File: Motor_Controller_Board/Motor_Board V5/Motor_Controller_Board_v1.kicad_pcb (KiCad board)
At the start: 2 copper layers, 74 x 89 mm, 105 parts, among them J201 Conn_01x02, J202 Conn_01x02, J203 Conn_01x02, J206 Conn_01x02, J207 Conn_01x02, J301 Conn_01x04, J302 USB_B_Micro, J303 Conn_01x02, J304 Conn_01x02, J305 Conn_01x02, J401 Conn_01x04, J402 Conn_01x04, J403 Conn_01x04, SW301 SW_Push, SW302 SW_Push, U201 TP6841S6, U202 AMS1117, U301 ESP32-C6-MINI-1, U401 A4988, U402 A4988, U403 A4988

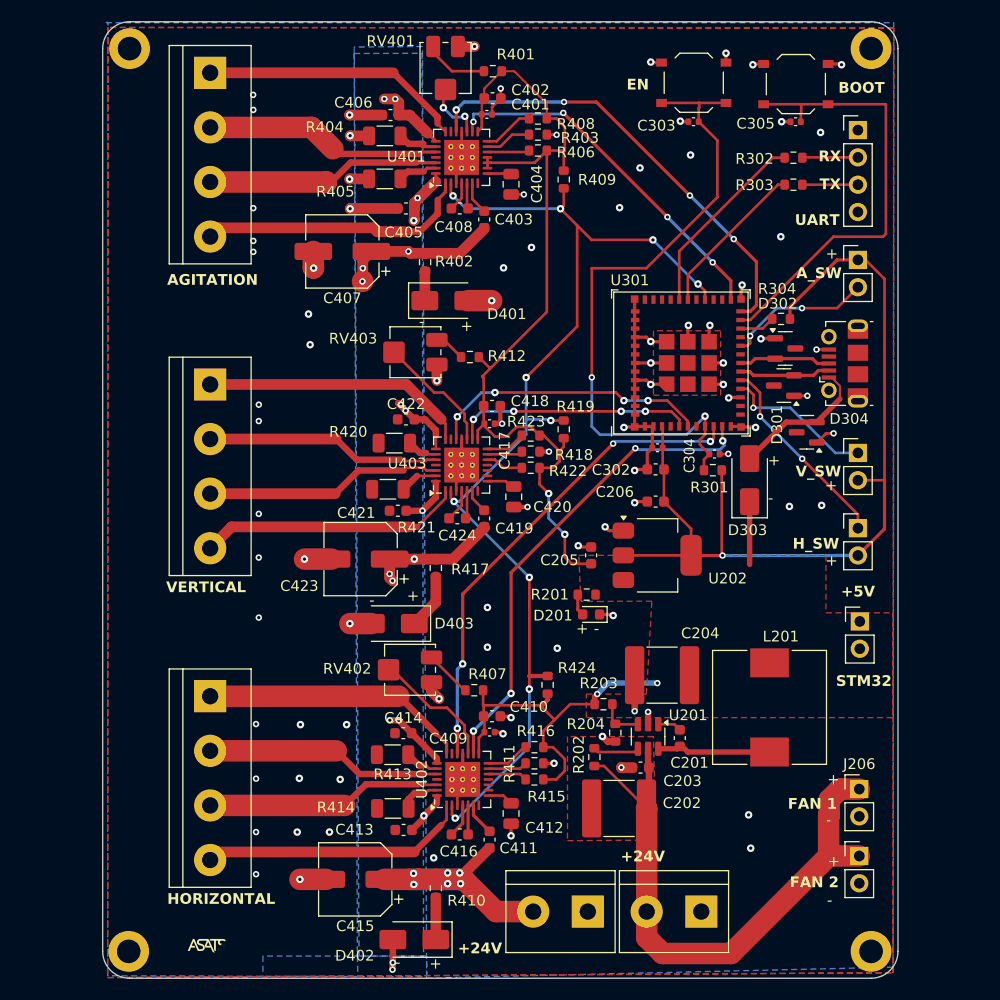
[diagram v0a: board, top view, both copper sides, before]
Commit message: cleaned up board and switched to horizontal text
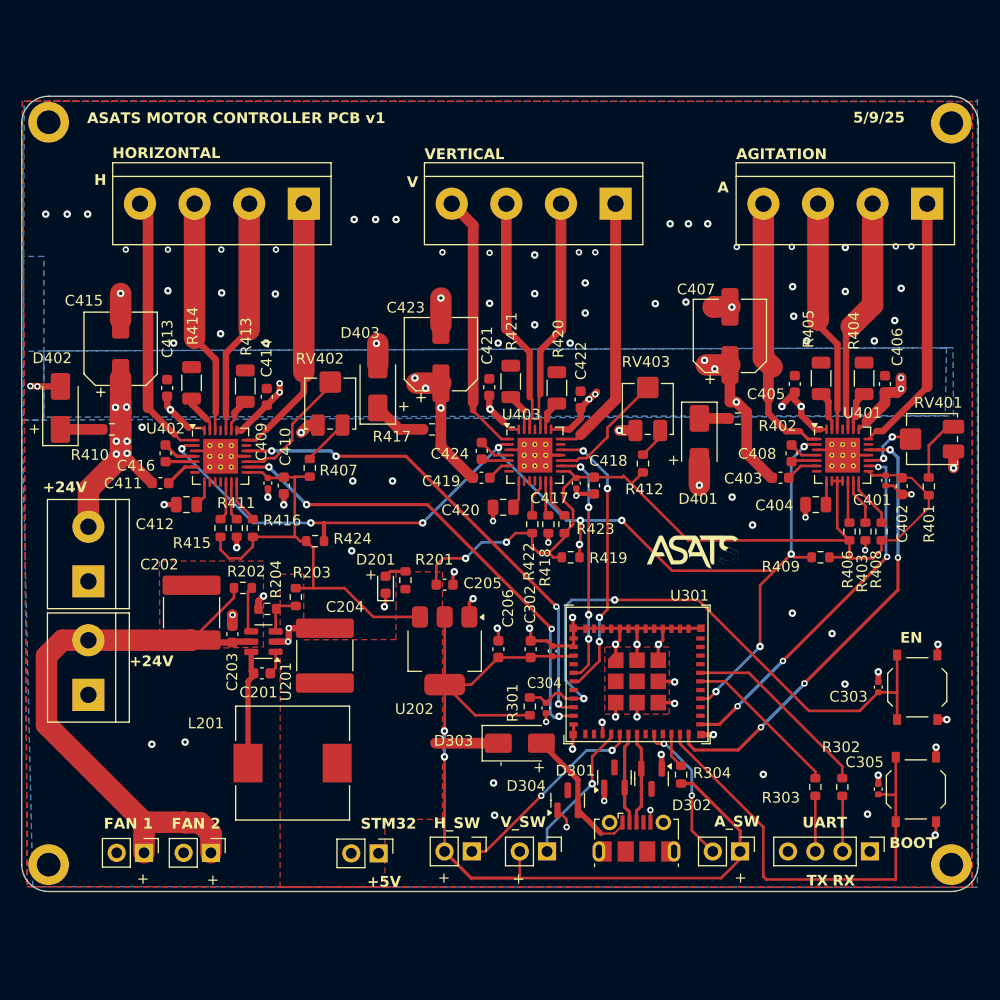
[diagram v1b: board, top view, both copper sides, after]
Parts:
- moved H204 77.5 mm to (109.0, 77.3), turned to -90 degrees
- moved H203 77.0 mm to (109.0, 146.4), turned to -90 degrees
- moved H201 76.8 mm to (193.0, 77.4), turned to -90 degrees
- moved H202 76.3 mm to (193.0, 146.4), turned to -90 degrees
- moved J401 67.8 mm to (190.7, 84.9), turned to 180 degrees
- moved J301 67.1 mm to (185.4, 145.2), turned to -90 degrees
- moved SW302 66.6 mm to (189.7, 139.4), turned to -90 degrees
- moved J207 66.6 mm to (117.8, 145.3), turned to -90 degrees
- moved C305 62.6 mm to (186.2, 139.4), turned to -90 degrees
- moved J206 60.6 mm to (124.1, 145.3), turned to -90 degrees
- moved J201 60.5 mm to (112.7, 130.6), turned to 90 degrees
- moved SW301 60.0 mm to (189.8, 129.9), turned to -90 degrees
- moved D402 59.4 mm to (110.1, 103.9), turned to 90 degrees
- moved R302 58.7 mm to (182.8, 139.2), turned to -90 degrees
- moved G*** 58.1 mm to (168.8, 117.4)
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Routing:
- net GND: track 126.9 -> 116.9 mm, vias 92 -> 111
- net +5V: track 125.7 -> 130.7 mm, vias 4 -> 2
- net /Microcontroller/EN: track 62.1 -> 57.3 mm
- net +24V: track 83.8 -> 87.3 mm
- net +3.3V: track 84.7 -> 85.8 mm, vias 1 -> 2
- net /Microcontroller/VERTICAL_SWITCH: track 14.1 -> 13.4 mm
- net DRIVER_ENABLE: vias 10 -> 11
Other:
- board size 74 x 89 mm -> 89 x 74 mm
- board text added: "5/9/25"
- board text added: "A"
- board text added: "ASATS MOTOR CONTROLLER PCB v1"
- board text added: "H"
- board text added: "V"

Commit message: done. see readme for update log
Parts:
- R401, R407, R412: value 24k -> 15k
- R404, R405, R413, R414, R420, R421: value 75m -> 100m
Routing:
- net GND: track 116.9 -> 116.6 mm, vias 111 -> 116
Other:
- board text removed: "-"
